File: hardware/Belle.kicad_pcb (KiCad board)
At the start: 2 copper layers, 53.8 x 57.4 mm, 16 parts, among them P1 Bell CONN, P2 Battery CONN, P3 Flashing CONN, U1 74AHC1G14, U2 ESP-12, U3 AP2112

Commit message: regenerated gerbers
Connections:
- C2 pad 2: Net-(C2-Pad2) -> +3V3
- SP1 pad 2: Net-(C2-Pad2) -> +3V3
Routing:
- net Net-(C2-Pad2): track 29.7 -> 0.00 mm
- net +3V3: track 0.00 -> 29.7 mm
- net GND: track 47.9 -> 37.8 mm, vias 5 -> 7
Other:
- board size 53.8 x 57.4 mm -> 46.7 x 57.4 mm

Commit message: edit layout. close #1
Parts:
- added C3: 1u, Capacitors_SMD:C_1206_HandSoldering, F.Cu at (133.2, 118.4)
- added C4: 1u, Capacitors_SMD:C_1206_HandSoldering, F.Cu at (122.6, 124.5)
- moved C2 38.4 mm to (104.0, 108.7), turned to 270 degrees
- moved R1 35.2 mm to (104.1, 117.6), turned to 270 degrees
- moved P1 22.4 mm to (101.1, 127.4), turned to 270 degrees
- moved P2 19.3 mm to (138.6, 131.6), turned to 270 degrees
- moved R4 12.5 mm to (128.0, 118.4)
- moved C1 12.0 mm to (119.5, 131.2), turned to 0 degrees
- moved R6 11.8 mm to (132.3, 105.3)
- moved U3 11.5 mm to (128.8, 130.2)
- moved R7 10.3 mm to (136.6, 87.8)
- moved U1 10.2 mm to (113.8, 120.9), turned to 180 degrees
- moved R3 10.0 mm to (103.6, 97.2)
- moved U2 5.07 mm to (113.0, 94.6)
- moved SP1 4.22 mm to (102.9, 87.5)
- moved R2 3.45 mm to (111.6, 131.2), turned to 180 degrees
- moved P3 2.84 mm to (140.5, 92.5)
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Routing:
- net +3V3: track 29.7 -> 0.00 mm
- net /5V: track 38.6 -> 60.0 mm, vias 0 -> 1
- net GND: track 37.8 -> 20.4 mm, vias 7 -> 9
- net Net-(SP1-Pad1): track 52.9 -> 45.5 mm
- net Net-(R5-Pad2): track 29.6 -> 36.2 mm, vias 0 -> 2
- net Net-(R6-Pad2): track 11.9 -> 5.58 mm
- net /FLASH_EN_1: track 11.3 -> 5.00 mm
- net Net-(C1-Pad1): track 24.6 -> 18.5 mm
- net Net-(P1-Pad2): track 28.7 -> 24.7 mm
- net Net-(R3-Pad1): track 7.97 -> 10.8 mm
- net /TX: track 14.9 -> 15.7 mm
- net /RX: track 15.1 -> 15.9 mm
- net Net-(R4-Pad1): track 13.2 -> 12.7 mm, vias 2 -> 0
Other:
- board text added: "5V"
- board text added: "EN1"
- board text added: "EN2"
- board text added: "GND"
- board text added: "RX"
- board text added: "TX"
- board text added: "V1.0 (https://github.com/sayanee/belle)"

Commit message: rename speaker to buzzer. close #9
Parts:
- SP1: value SPEAKER -> BUZZER
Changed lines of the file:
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@@
-(kicad_pcb (version 4) (host pcbnew 4.0.2-stable)
+(kicad_pcb (version 4) (host pcbnew 4.0.5)
   (general
     (links 38)
     (no_connects 0)
-    (area 94.067 77.394999 143.331001 135.306001)
+    (area 96.444999 77.394999 143.331001 134.949001)
     (thickness 1.6)
     (drawings 13)
@@
       (effects (font (size 1 1) (thickness 0.15)))
     )
-    (fp_text value SPEAKER (at 0 5.588) (layer F.Fab)
+    (fp_text value BUZZER (at 0 5.588) (layer F.Fab)
       (effects (font (size 1 1) (thickness 0.15)))
     )
@@
   (segment (start 124.333 108.712) (end 124.333 112.681) (width 0.25) (layer F.Cu) (net 10))
   (segment (start 124.333 112.681) (end 128.016 116.364) (width 0.25) (layer F.Cu) (net 10))
-  (segment (start 126.7648 83.9216) (end 127.8128 83.9216) (width 0.25) (layer F.Cu) (net 11) (status 400000))
-  (segment (start 129.2174 104.615) (end 127.03 104.615) (width 0.25) (layer F.Cu) (net 11) (status 800000))
+  (segment (start 126.7648 83.9216) (end 127.8128 83.9216) (width 0.25) (layer F.Cu) (net 11))
+  (segment (start 129.2174 104.615) (end 127.03 104.615) (width 0.25) (layer F.Cu) (net 11))
   (segment (start 130.5052 103.3272) (end 129.2174 104.615) (width 0.25) (layer F.Cu) (net 11))
   (via (at 130.5052 103.3272) (size 0.6) (drill 0.4) (layers F.Cu B.Cu) (net 11))

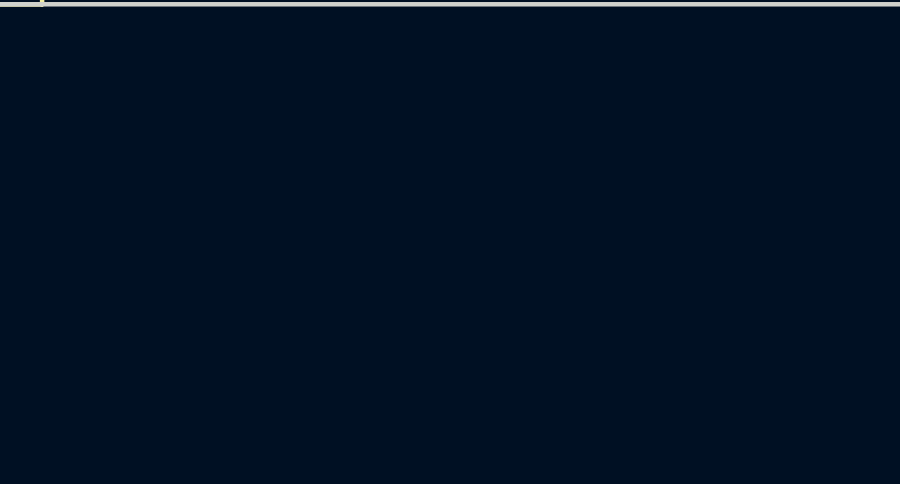
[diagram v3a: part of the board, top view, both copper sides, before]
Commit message: re-generate net list based on new schematic
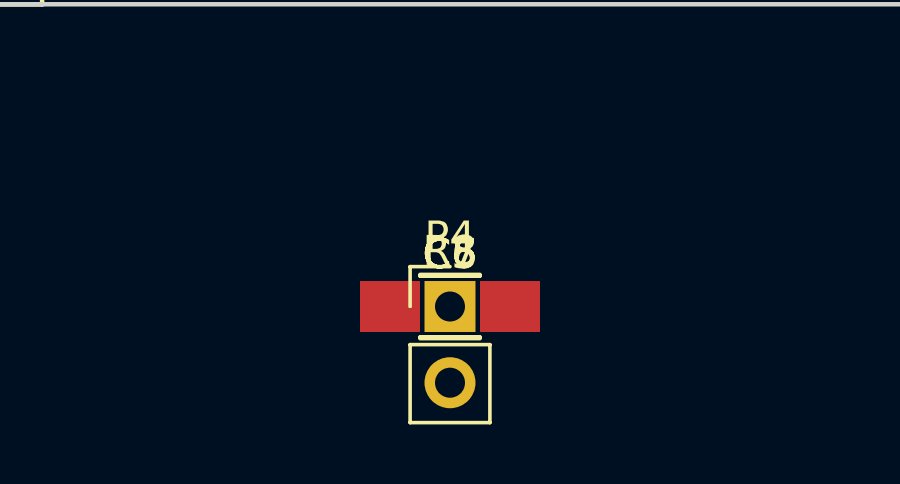
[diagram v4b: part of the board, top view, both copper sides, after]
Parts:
- added C5, C6, C7: DNP, Capacitors_SMD:C_1206_HandSoldering, F.Cu at (119.9, 144.9)
- added P4: Boot JUMPER, Pin_Headers:Pin_Header_Straight_1x02_Pitch2.54mm, F.Cu at (119.9, 144.9)
- added R8: 10K, Resistors_SMD:R_1206_HandSoldering, F.Cu at (119.9, 144.9)
- P3: value Flashing CONN -> FTDI Flashing CONN
- R2: value 51k -> 47k
- R3, R6: value 12K -> 10K
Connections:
- P1 pad 1: GND -> +3V3
- P3 pad 1: /FLASH_EN_1 -> GND
- P3 pad 2: GND -> /CTS
- P3 pad 6: GND -> /DTR
- R1 pad 1: +3V3 -> GND
- SP1 pad 1: Net-(SP1-Pad1) -> Net-(R8-Pad1)
- U1 pad 4: Net-(SP1-Pad1) -> Net-(R8-Pad2)
- U2 pad 1: Net-(SP1-Pad1) -> Net-(R8-Pad1)
- U2 pad 13: Net-(U2-Pad13) -> /DTR
- U2 pad 14: Net-(U2-Pad14) -> /CTS
- U2 pad 15: /RX -> /TX
- U2 pad 16: /TX -> /RX
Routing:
- net Net-(SP1-Pad1): track 45.5 -> 0.00 mm
- net Net-(R8-Pad2): track 0.00 -> 25.7 mm
- net Net-(R8-Pad1): track 0.00 -> 19.8 mm
- net /FLASH_EN_1: track 5.00 -> 1.29 mm
- net +3V3: track 0.00 -> 2.72 mm, vias 0 -> 1
- net GND: track 20.4 -> 21.4 mm, vias 9 -> 8
- net /RX: track 15.9 -> 16.5 mm
- net /TX: track 15.7 -> 15.2 mm

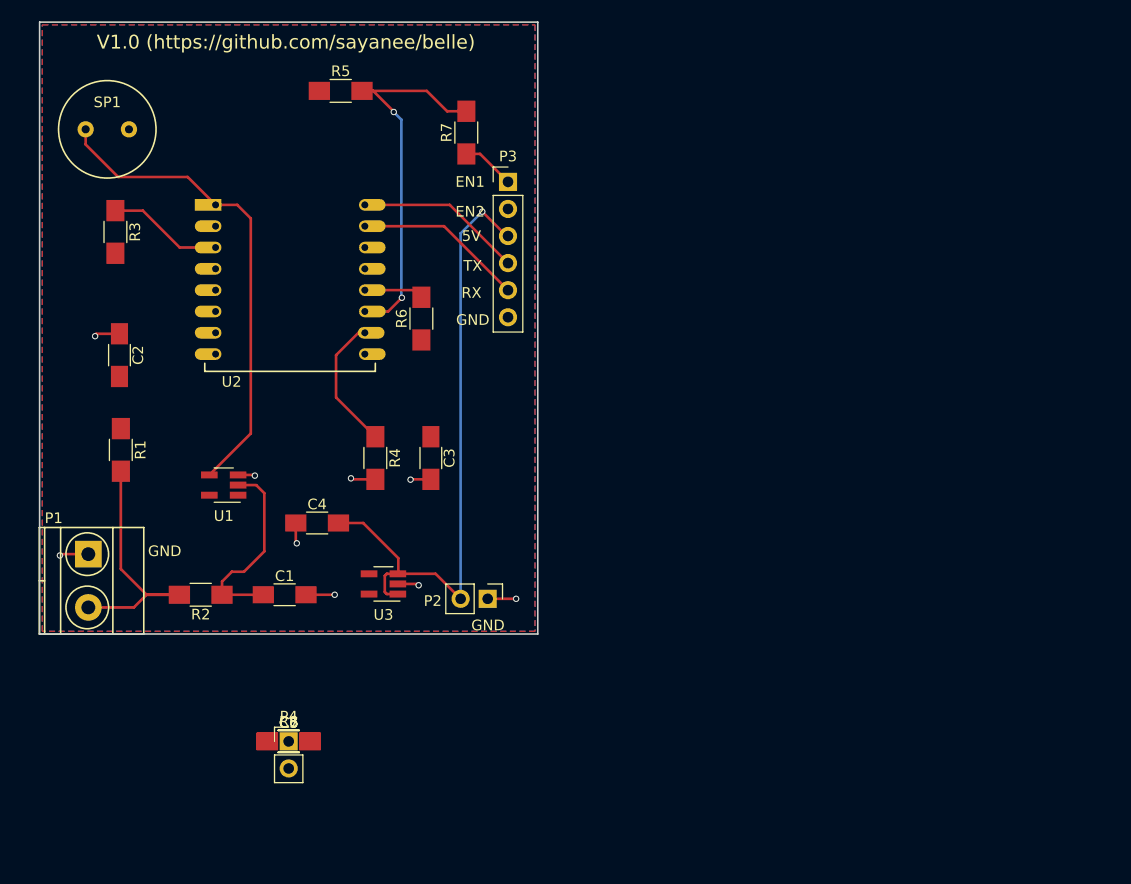
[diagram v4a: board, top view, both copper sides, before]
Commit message: initial rat's nest. #2 #10
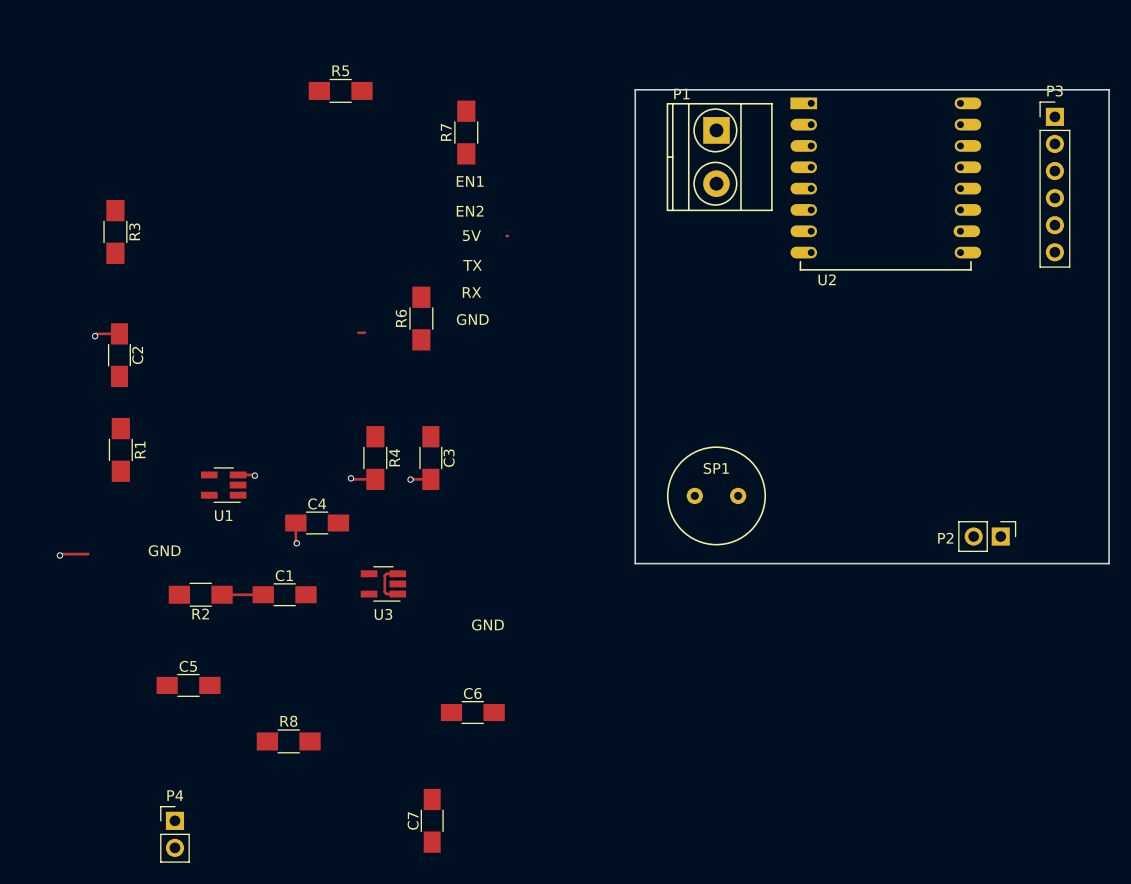
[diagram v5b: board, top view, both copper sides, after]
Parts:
- R5: value 12K -> 10K
- R7: value 470R -> 10K
- moved P1 71.1 mm to (160.0, 87.6)
- moved SP1 66.7 mm to (160.0, 121.9)
- moved U2 56.7 mm to (168.9, 85.1)
- moved P3 51.7 mm to (191.8, 86.4)
- moved P2 48.5 mm to (186.7, 125.7)
- moved C6 17.5 mm to (137.2, 142.2)
- moved C7 15.4 mm to (133.3, 152.4), turned to 90 degrees
- moved P4 13.0 mm to (109.2, 152.4)
- moved C5 10.8 mm to (110.5, 139.7)
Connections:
- R4 pad 2: GND -> Net-(R4-Pad2)
- R5 pad 1: +3V3 -> Net-(R5-Pad1)
- R5 pad 2: Net-(R5-Pad2) -> GND
- R6 pad 2: Net-(P4-Pad1) -> Net-(R6-Pad2)
- R7 pad 1: /FLASH_EN_1 -> +3V3
- R7 pad 2: Net-(R5-Pad2) -> Net-(P4-Pad1)
- SP1 pad 1: Net-(R8-Pad1) -> Net-(R4-Pad1)
- U1 pad 4: Net-(R8-Pad2) -> Net-(R4-Pad2)
- U2 pad 1: Net-(R8-Pad1) -> Net-(R4-Pad1)
- U2 pad 10: Net-(R4-Pad1) -> Net-(R5-Pad1)
- U2 pad 11: Net-(R5-Pad2) -> Net-(R6-Pad2)
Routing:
- net /5V: track 60.0 -> 4.19 mm, vias 1 -> 0
- net Net-(R5-Pad2): track 36.2 -> 0.00 mm, vias 2 -> 0
- net Net-(R8-Pad2): track 25.7 -> 0.00 mm
- net Net-(P1-Pad2): track 24.7 -> 0.00 mm
- net Net-(R8-Pad1): track 19.8 -> 0.00 mm
- net /RX: track 16.5 -> 0.00 mm
- net /TX: track 15.2 -> 0.00 mm
- net Net-(C1-Pad1): track 18.5 -> 3.87 mm
- net GND: track 21.4 -> 7.91 mm, vias 8 -> 4
- net Net-(R4-Pad1): track 12.7 -> 0.00 mm
- net Net-(R3-Pad1): track 10.8 -> 0.00 mm
- net Net-(P4-Pad1): track 5.58 -> 0.00 mm
- net (no net): track 0.00 -> 3.45 mm, vias 0 -> 1
- net +3V3: track 2.72 -> 0.00 mm, vias 1 -> 0
- net Net-(R4-Pad2): track 0.00 -> 2.33 mm, vias 0 -> 1
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- removed copper zone on F.Cu, net +3V3
- removed copper zone on B.Cu, net GND
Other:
- board size 46.7 x 57.4 mm -> 44.4 x 44.5 mm
- board text removed: "V1.0 (https://github.com/sayanee/belle)"

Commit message: layout PCB
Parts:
- removed R8: 10K, Resistors_SMD:R_1206_HandSoldering
- added REF**: M3, Mounting_Holes:MountingHole_3.2mm_M3, F.Cu at (159.4, 100.3)
- added REF**: M3, Mounting_Holes:MountingHole_3.2mm_M3, F.Cu at (189.9, 100.3)
- C2: value 10uF -> 10u
- P2: value Battery CONN -> Battery
- moved P4 100.1 mm to (188.6, 91.4), turned to 90 degrees
- moved C5 72.8 mm to (174.0, 104.1), turned to 180 degrees
- moved R1 67.3 mm to (171.4, 118.7), turned to 180 degrees
- moved R5 66.1 mm to (189.9, 95.2)
- moved R3 59.6 mm to (163.2, 94.6)
- moved C4 59.1 mm to (181.6, 125.7), turned to 180 degrees
- moved C2 57.4 mm to (161.3, 105.4), turned to 180 degrees
- moved C7 57.1 mm to (181.6, 121.9), turned to 180 degrees
- moved R6 56.9 mm to (189.2, 105.4), turned to 180 degrees
- moved C6 55.9 mm to (182.2, 109.2)
- moved C1 55.2 mm to (172.1, 114.3)
- moved U3 55.0 mm to (182.2, 117.5)
- moved R7 53.3 mm to (189.9, 86.4), turned to 180 degrees
- moved R2 50.4 mm to (159.4, 114.9), turned to 0 degrees
- moved C3 49.3 mm to (182.2, 113.0), turned to 0 degrees
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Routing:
- net /CTS: track 0.00 -> 47.7 mm, vias 0 -> 2
- net /RX: track 0.00 -> 39.3 mm, vias 0 -> 2
- net Net-(R4-Pad1): track 0.00 -> 36.7 mm
- net /TX: track 0.00 -> 35.4 mm, vias 0 -> 2
- net /DTR: track 0.00 -> 31.9 mm, vias 0 -> 2
- net /5V: track 4.19 -> 31.3 mm
- net GND: track 7.91 -> 33.5 mm, vias 4 -> 11
- net Net-(C1-Pad1): track 3.87 -> 25.3 mm
- net Net-(P1-Pad2): track 0.00 -> 17.0 mm
- net Net-(R6-Pad2): track 0.94 -> 17.7 mm
- net Net-(P4-Pad1): track 0.00 -> 13.3 mm
- net Net-(R5-Pad1): track 0.00 -> 7.25 mm
- net Net-(R3-Pad1): track 0.00 -> 6.70 mm
- net Net-(R4-Pad2): track 2.33 -> 6.20 mm, vias 1 -> 0
- net (no net): track 3.45 -> 0.13 mm, vias 1 -> 0
- added copper zone on F.Cu, net +3V3
- added copper zone on B.Cu, net GND
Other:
- net class Default: clearance 0.2 -> 0.254; trace_width 0.25 -> 0.254; via_dia 0.6 -> 0.6858; via_drill 0.4 -> 0.3302
- rule trace_clearance: 0.2 -> 0.254
- rule trace_min: 0.2 -> 0.1524
- rule via_min_drill: 0.3 -> 0.3302
- rule via_min_size: 0.4 -> 0.6858
- board text added: "CTS"
- board text added: "DTR"
- board text removed: "EN1"
- board text removed: "EN2"

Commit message: adjust decoupling capacitors
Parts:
- C2: value 10u -> DNP
- C4: value 1u -> DNP
- C5: value DNP -> 10u
- C7: value DNP -> 1u
- P2: value Battery -> Battery CONN
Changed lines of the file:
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@@
   (layers
     (0 F.Cu signal)
-    (31 B.Cu signal)
+    (31 B.Cu signal hide)
     (32 B.Adhes user)
     (33 F.Adhes user)
@@
       (effects (font (size 1 1) (thickness 0.15)))
     )
-    (fp_text value 10u (at -5.08 0 180) (layer F.Fab)
+    (fp_text value DNP (at -5.08 0 180) (layer F.Fab)
       (effects (font (size 1 1) (thickness 0.15)))
     )
@@
       (effects (font (size 1 1) (thickness 0.15)))
     )
-    (fp_text value Battery (at 2.54 1.27 180) (layer F.Fab)
+    (fp_text value "Battery CONN" (at 2.54 1.27 180) (layer F.Fab)
       (effects (font (size 1 1) (thickness 0.15)))
     )
@@
       (effects (font (size 1 1) (thickness 0.15)))
     )
-    (fp_text value 1u (at -4.445 0 180) (layer F.Fab)
+    (fp_text value DNP (at -4.445 0 180) (layer F.Fab)
       (effects (font (size 1 1) (thickness 0.15)))
     )
@@
       (effects (font (size 1 1) (thickness 0.15)))
     )
-    (fp_text value DNP (at -5.08 0 180) (layer F.Fab)
+    (fp_text value 10u (at -5.08 0 180) (layer F.Fab)
       (effects (font (size 1 1) (thickness 0.15)))
     )
@@
       (effects (font (size 1 1) (thickness 0.15)))
     )
-    (fp_text value DNP (at -5.08 0 360) (layer F.Fab)
+    (fp_text value 1u (at -5.08 0 360) (layer F.Fab)
       (effects (font (size 1 1) (thickness 0.15)))
     )
@@
     (descr "Through hole straight pin header, 1x02, 2.54mm pitch, single row")
     (tags "Through hole pin header THT 1x02 2.54mm single row")
-    (fp_text reference P4 (at 0 -2.33 180) (layer F.SilkS)
+    (fp_text reference P4 (at 0 -3.175 180) (layer F.SilkS)
       (effects (font (size 1 1) (thickness 0.15)))
     )
@@
   (segment (start 167.545 111.76) (end 170.085 114.3) (width 0.254) (layer F.Cu) (net 1))
   (segment (start 160.02 111.76) (end 167.545 111.76) (width 0.254) (layer F.Cu) (net 1))
-  (segment (start 191.865 95.25) (end 192.405 95.25) (width 0.254) (layer F.Cu) (net 2) (status C00000))
-  (segment (start 192.405 95.25) (end 194.31 93.345) (width 0.254) (layer F.Cu) (net 2) (status 400000))
+  (segment (start 191.865 95.25) (end 192.405 95.25) (width 0.254) (layer F.Cu) (net 2))
+  (segment (start 192.405 95.25) (end 194.31 93.345) (width 0.254) (layer F.Cu) (net 2))
   (via (at 194.31 93.345) (size 0.6858) (drill 0.3302) (layers F.Cu B.Cu) (net 2))
   (segment (start 163.29 105.41) (end 163.29 104.045) (width 0.254) (layer F.Cu) (net 2))
@@
   (segment (start 159.465 110.17) (end 163.42 110.17) (width 0.254) (layer F.Cu) (net 19))
   (segment (start 163.42 110.17) (end 165.005 108.585) (width 0.254) (layer F.Cu) (net 19))
-  (segment (start 181.64 97.725) (end 185.355 97.725) (width 0.254) (layer F.Cu) (net 20) (status 400000))
-  (segment (start 185.355 97.725) (end 187.83 95.25) (width 0.254) (layer F.Cu) (net 20) (status 800000))
-  (segment (start 187.83 95.25) (end 187.865 95.25) (width 0.254) (layer F.Cu) (net 20) (status C00000))
+  (segment (start 181.64 97.725) (end 185.355 97.725) (width 0.254) (layer F.Cu) (net 20))
+  (segment (start 185.355 97.725) (end 187.83 95.25) (width 0.254) (layer F.Cu) (net 20))
+  (segment (start 187.83 95.25) (end 187.865 95.25) (width 0.254) (layer F.Cu) (net 20))
   (segment (start 181.64 95.725) (end 179.865 95.725) (width 0.254) (layer F.Cu) (net 21))
   (segment (start 182.88 105.41) (end 187.23 105.41) (width 0.254) (layer F.Cu) (net 21))

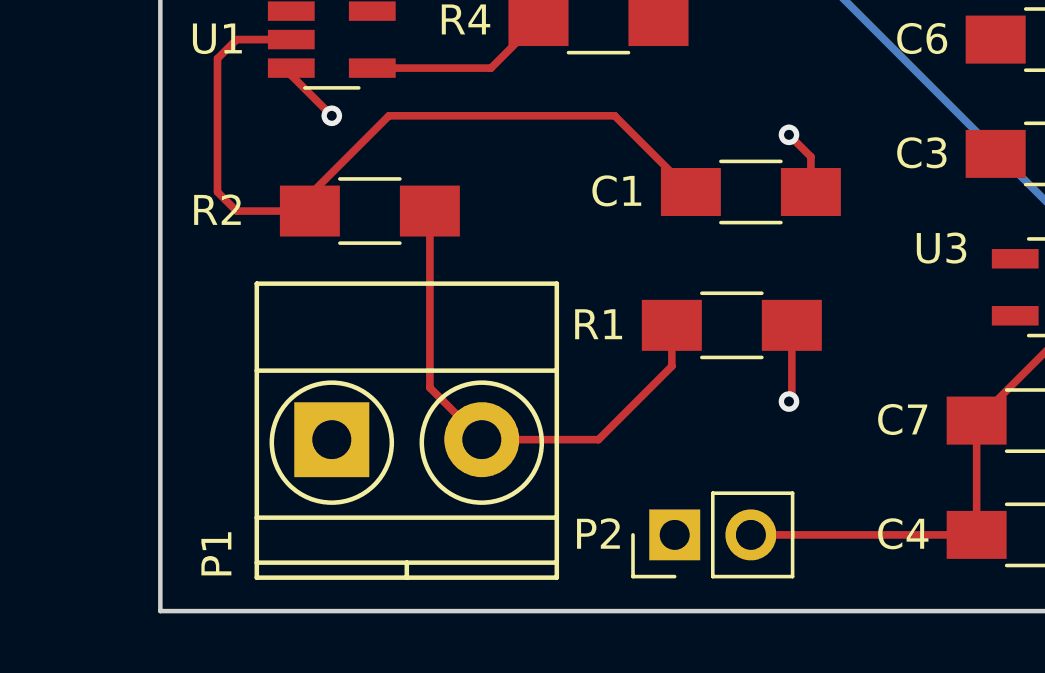
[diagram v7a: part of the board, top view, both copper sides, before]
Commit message: add labels for battery connecter
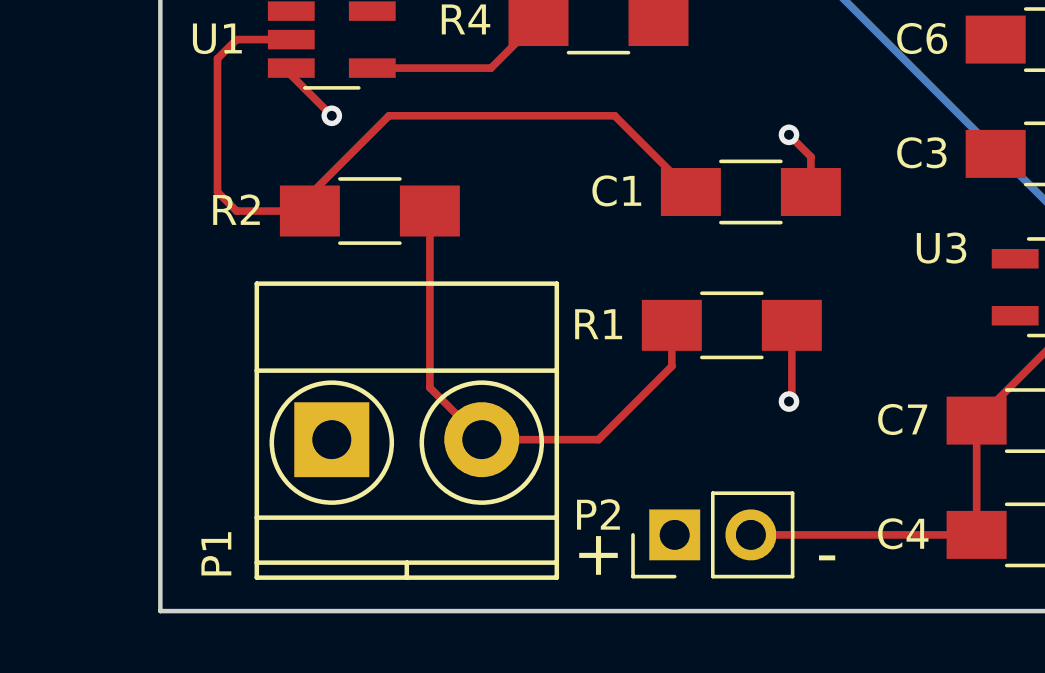
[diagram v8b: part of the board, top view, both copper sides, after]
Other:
- board text added: "+"
- board text added: "-"
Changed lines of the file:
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@@
     (area 152.324999 83.744999 196.925001 128.345001)
     (thickness 1.6)
-    (drawings 10)
+    (drawings 12)
     (tracks 123)
     (zones 0)
@@
   (layers
     (0 F.Cu signal)
-    (31 B.Cu signal hide)
+    (31 B.Cu signal)
     (32 B.Adhes user)
     (33 F.Adhes user)
@@
     (descr "Through hole straight pin header, 1x02, 2.54mm pitch, single row")
     (tags "Through hole pin header THT 1x02 2.54mm single row")
-    (fp_text reference P2 (at 0 -2.54 180) (layer F.SilkS)
+    (fp_text reference P2 (at 0.635 -2.54 180) (layer F.SilkS)
       (effects (font (size 1 1) (thickness 0.15)))
     )
@@
     (tags "resistor 1206")
     (attr smd)
-    (fp_text reference R2 (at -5.08 0) (layer F.SilkS)
+    (fp_text reference R2 (at -4.445 0) (layer F.SilkS)
       (effects (font (size 1 1) (thickness 0.15)))
     )
@@
     (pad 1 np_thru_hole circle (at 0 0) (size 3.2 3.2) (drill 3.2) (layers *.Cu *.Mask))
   )
+  (gr_text - (at 174.625 126.365) (layer F.SilkS)
+    (effects (font (size 1.5 1.5) (thickness 0.3)))
+  )
+  (gr_text + (at 167.005 126.365) (layer F.SilkS)
+    (effects (font (size 1.5 1.5) (thickness 0.3)) (justify mirror))
+  )
   (gr_text RX (at 191.77 113.665) (layer F.SilkS)
